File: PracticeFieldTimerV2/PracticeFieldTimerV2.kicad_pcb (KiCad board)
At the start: 2 copper layers, 99 x 96 mm, 37 parts, among them J1 External Controls, J2 Screw_Terminal_01x04, J3 Panel, J5 /CAN Enable, J6 RJ45-B, J7 RJ45-A, U1 ESP32-DevKitC, U4 DS3231MZ_TRL, U5 SN65HVD230DR

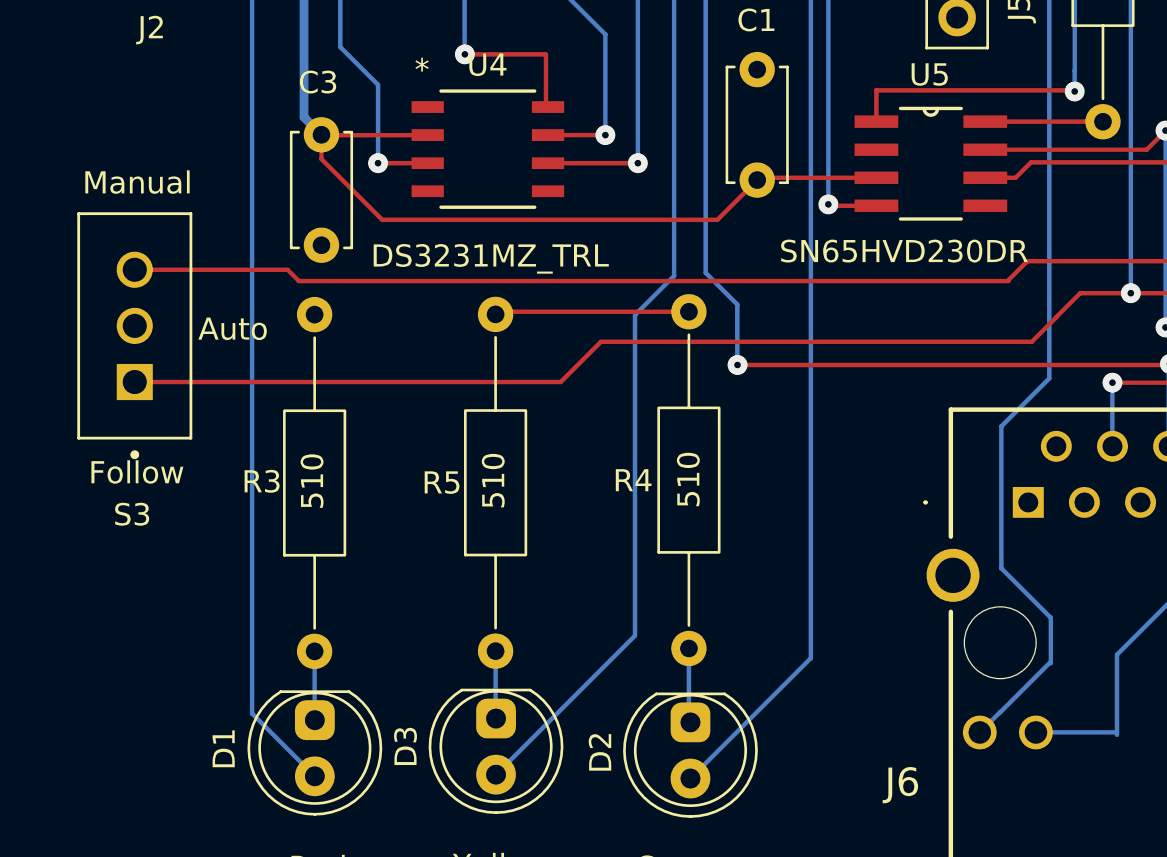
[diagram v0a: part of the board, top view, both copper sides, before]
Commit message: Add 10K pullup to SQW per DS3231 datasheet. Silly me!
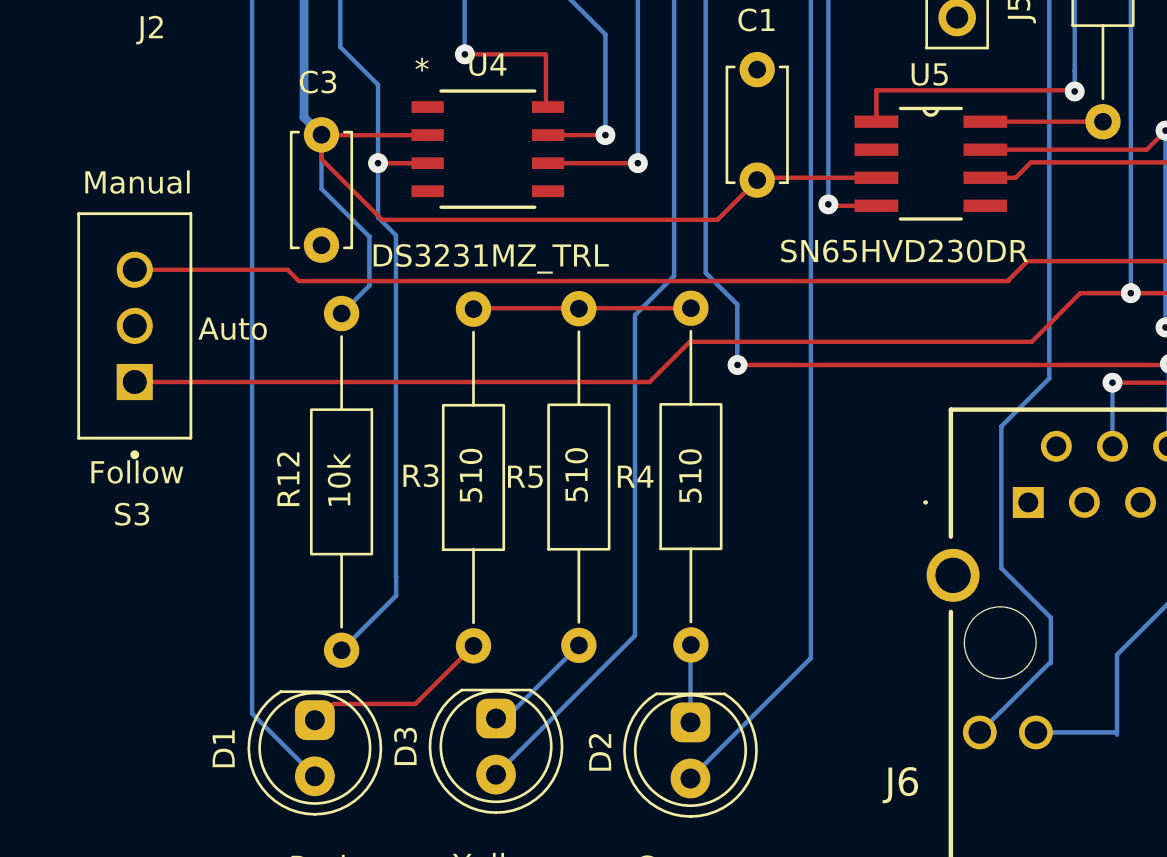
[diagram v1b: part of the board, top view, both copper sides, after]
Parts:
- added R12: 10k, Resistor_THT:R_Axial_DIN0207_L6.3mm_D2.5mm_P15.24mm_Horizontal, F.Cu at (63.5, 91.0)
- moved R3 7.19 mm to (69.5, 106.0)
- moved R5 3.78 mm to (74.2, 106.0)
- moved R4 0.18 mm to (79.3, 106.0)
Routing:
- net SQW: track 52.8 -> 76.2 mm
- net +3.3V: track 89.8 -> 99.3 mm
- net Net-(D1-K): track 3.10 -> 8.46 mm
- net Net-(D3-K): track 3.03 -> 4.68 mm
- net GND: track 8.62 -> 9.65 mm

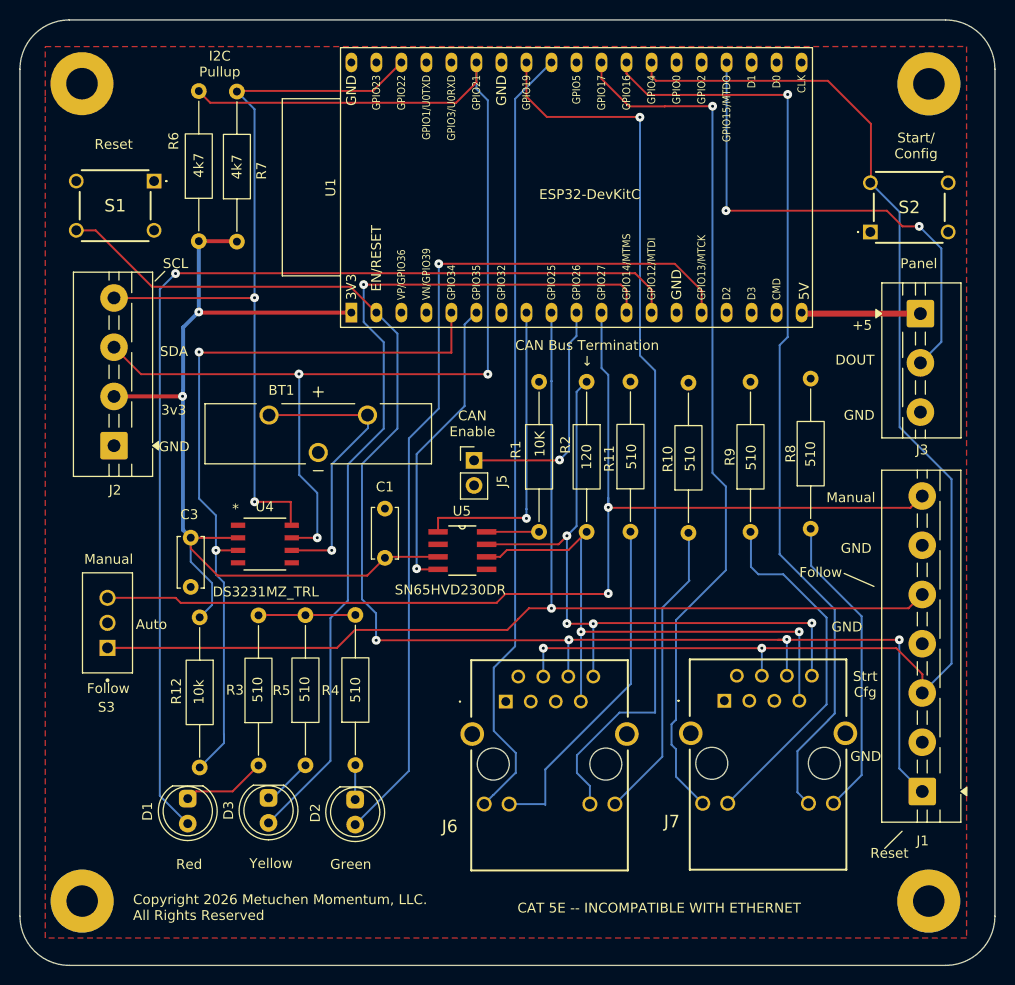
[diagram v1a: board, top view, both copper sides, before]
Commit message: Adjust traces to neaten layout a bit. Add bridge to unfilled area. Add meaningful reference codes to the mounting holes to eliminate duplicate footprint warnings.
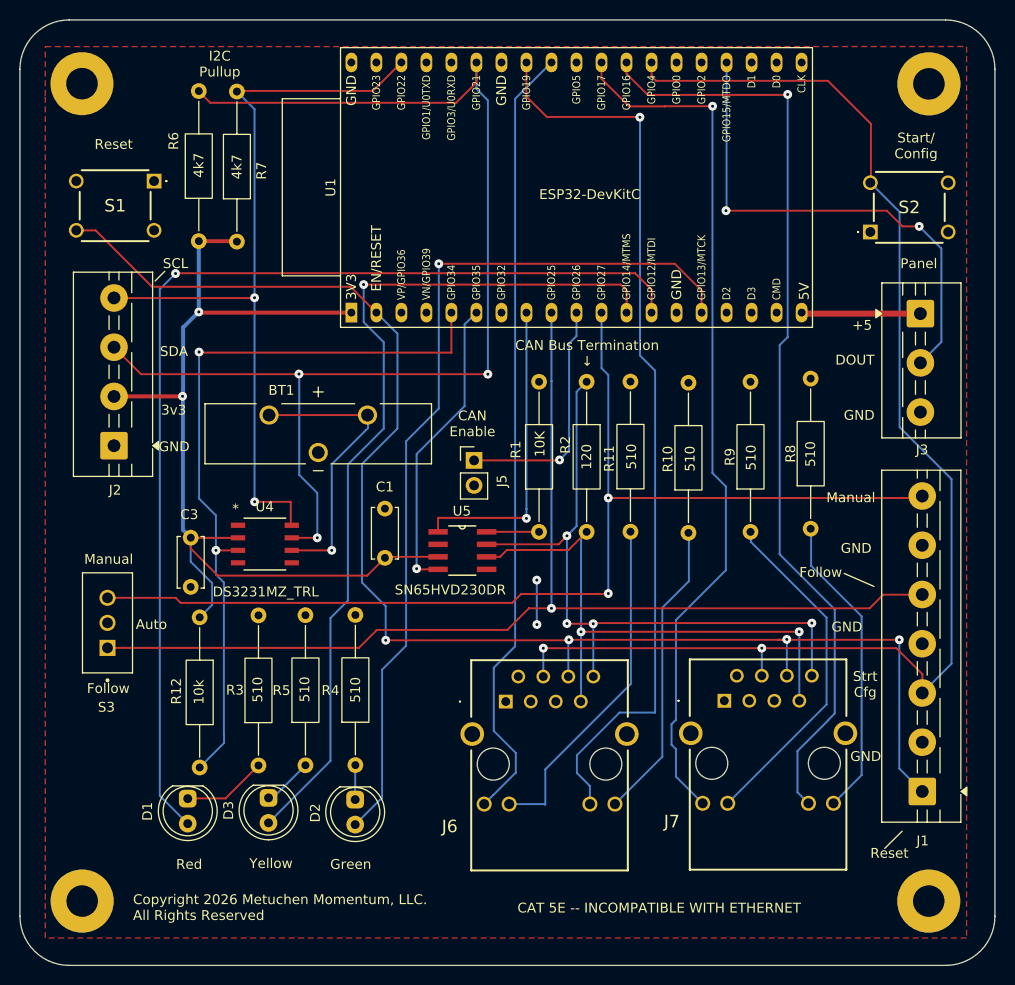
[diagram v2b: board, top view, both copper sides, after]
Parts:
- renumbered REF** to MH1, REF** to MH2, REF** to MH3, REF** to MH4
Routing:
- net GND: track 9.65 -> 4.54 mm, vias 0 -> 2
- net /Manual: track 113.1 -> 111.5 mm
- net Net-(J7-K_YELLOW): track 35.9 -> 34.4 mm
- net /RST: track 148.5 -> 148.0 mm
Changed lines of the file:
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@@
 		(descr "Mounting Hole 3.2mm, M3, generated by kicad-footprint-generator mountinghole.py")
 		(tags "mountinghole M3")
-		(property "Reference" "REF**"
+		(property "Reference" "MH2"
 			(at 0 -4.15 0)
 			(layer "F.SilkS")
@@
 		(descr "Mounting Hole 3.2mm, M3, generated by kicad-footprint-generator mountinghole.py")
 		(tags "mountinghole M3")
-		(property "Reference" "REF**"
+		(property "Reference" "MH3"
 			(at 0 -4.15 0)
 			(layer "F.SilkS")
@@
 		(descr "Mounting Hole 3.2mm, M3, generated by kicad-footprint-generator mountinghole.py")
 		(tags "mountinghole M3")
-		(property "Reference" "REF**"
+		(property "Reference" "MH1"
 			(at 0 -4.15 0)
 			(layer "F.SilkS")
@@
 		(descr "Mounting Hole 3.2mm, M3, generated by kicad-footprint-generator mountinghole.py")
 		(tags "mountinghole M3")
-		(property "Reference" "REF**"
+		(property "Reference" "MH4"
 			(at 0 -4.15 0)
 			(layer "F.SilkS")
@@
 		(net 1)
 	)
+	(via
+		(at 97.74 87.19)
+		(size 0.9)
+		(drill 0.3)
+		(layers "F.Cu" "B.Cu")
+		(free yes)
+		(net 2)
+	)
+	(via
+		(at 97.75 91.7)
+		(size 0.9)
+		(drill 0.3)
+		(layers "F.Cu" "B.Cu")
+		(free yes)
+		(net 2)
+	)
 	(segment
-		(start 79.54 90.73)
-		(end 69.89 90.73)
+		(start 97.74 91.63)
+		(end 97.81 91.7)
 		(width 0.2)
-		(layer "F.Cu")
+		(layer "B.Cu")
 		(net 2)
 	)
 	(segment
-		(start 66.85 108.64)
-		(end 63.15 108.64)
+		(start 97.74 87.19)
+		(end 97.74 91.63)
 		(width 0.2)
-		(layer "F.Cu")
-		(net 3)
+		(layer "B.Cu")
+		(net 2)
 	)
 	(segment
-		(start 63.15 108.64)
-		(end 62.415 109.375)
+		(start 69.48 106.01)
+		(end 66.14 109.35)
 		(width 0.2)
 		(layer "F.Cu")
@@
 	)
 	(segment
-		(start 69.48 106.01)
-		(end 66.85 108.64)
+		(start 66.14 109.35)
+		(end 62.44 109.35)
 		(width 0.2)
 		(layer "F.Cu")
@@
 	)
 	(segment
-		(start 84.75 72.81)
-		(end 84.75 106.565)
+		(start 82.03 109.285)
+		(end 79.3 112.015)
+		(width 0.2)
+		(layer "B.Cu")
+		(net 5)
+	)
+	(segment
+		(start 84.47 93.85)
+		(end 82.03 96.29)
+		(width 0.2)
+		(layer "B.Cu")
+		(net 5)
+	)
+	(segment
+		(start 87.79 69.77)
+		(end 84.47 73.09)
 		(width 0.2)
 		(layer "B.Cu")
@@
 	)
 	(segment
-		(start 84.75 106.565)
-		(end 79.3 112.015)
+		(start 84.47 73.09)
+		(end 84.47 93.85)
 		(width 0.2)
 		(layer "B.Cu")
@@
 	)
 	(segment
-		(start 87.79 69.77)
-		(end 84.75 72.81)
+		(start 82.03 96.29)
+		(end 82.03 109.285)
 		(width 0.2)
 		(layer "B.Cu")
@@
 	)
 	(segment
-		(start 54.15 94.07)
-		(end 77.45 94.07)
+		(start 132.91 88.67)
+		(end 136.86 88.67)
 		(width 0.2)
 		(layer "F.Cu")
@@
 	)
 	(segment
-		(start 77.45 94.07)
-		(end 79.27 92.25)
+		(start 95.85 91.14)
+		(end 96.94 90.05)
+		(width 0.2)
+		(layer "F.Cu")
+		(net 9)
+	)
+	(segment
+		(start 54.15 94.07)
+		(end 79.67 94.07)
 		(width 0.2)
 		(layer "F.Cu")
@@
 	)
 	(segment
-		(start 99.23 90.05)
-		(end 135.480001 90.049999)
+		(start 96.94 90.05)
+		(end 99.23 90.05)
 		(width 0.2)
 		(layer "F.Cu")
@@
 	)
 	(segment
-		(start 79.27 92.25)
-		(end 94.75 92.25)
+		(start 131.53 90.05)
+		(end 132.91 88.67)
 		(width 0.2)
 		(layer "F.Cu")
@@
 	)
 	(segment
-		(start 95.85 91.15)
-		(end 95.85 91.14)
+		(start 79.67 94.07)
+		(end 81.49 92.25)
 		(width 0.2)
 		(layer "F.Cu")
@@
 	)
 	(segment
-		(start 135.480001 90.049999)
-		(end 136.88 88.65)
+		(start 99.23 90.05)
+		(end 131.53 90.05)
 		(width 0.2)
 		(layer "F.Cu")
@@
 	)
 	(segment
-		(start 96.94 90.05)
-		(end 99.23 90.05)
+		(start 95.85 91.15)
+		(end 95.85 91.14)
 		(width 0.2)
 		(layer "F.Cu")
@@
 	)
 	(segment
-		(start 95.85 91.14)
-		(end 96.94 90.05)
+		(start 81.49 92.25)
+		(end 94.75 92.25)
 		(width 0.2)
 		(layer "F.Cu")
@@
 	)
 	(segment
-		(start 61.07 88.99)
-		(end 61.58 89.5)
-		(width 0.2)
-		(layer "F.Cu")
-		(net 10)
-	)
-	(segment
 		(start 54.15 88.99)
 		(end 61.07 88.99)
@@
 	)
 	(segment
-		(start 94.55 88.6)
-		(end 93.7 89.45)
-		(width 0.2)
-		(layer "F.Cu")
-		(net 10)
-	)
-	(segment
-		(start 104.55 88.6)
-		(end 94.55 88.6)
+		(start 61.07 88.99)
+		(end 61.58 89.5)
 		(width 0.2)
 		(layer "F.Cu")
@@
 	)
 	(segment
-		(start 105.05 79.85)
-		(end 135.68 79.85)
+		(start 61.58 89.5)
+		(end 95.25 89.5)
 		(width 0.2)
 		(layer "F.Cu")
@@
 	)
 	(segment
-		(start 105 79.8)
-		(end 105.05 79.85)
+		(start 96.15 88.6)
+		(end 95.25 89.5)
 		(width 0.2)
 		(layer "F.Cu")
@@
 	)
 	(segment
-		(start 61.58 89.5)
-		(end 93.7 89.5)
+		(start 104.55 88.6)
+		(end 96.15 88.6)
 		(width 0.2)
 		(layer "F.Cu")
@@
 	)
 	(segment
-		(start 135.68 79.85)
-		(end 136.88 78.65)
+		(start 105 78.85)
+		(end 136.68 78.85)
 		(width 0.2)
 		(layer "F.Cu")
@@
 	)
 	(via
-		(at 105 79.8)
+		(at 105 78.85)
 		(size 0.9)
 		(drill 0.3)
@@
 	)
 	(segment
-		(start 105 79.8)
-		(end 105 78.85)
-		(width 0.2)
-		(layer "B.Cu")
-		(net 10)
-	)
-	(segment
 		(start 104.31272 65.66272)
 		(end 104.31272 60.02632)
@@
 	)
 	(segment
-		(start 81.43 93.3)
-		(end 100.95 93.3)
-		(width 0.2)
-		(layer "F.Cu")
-		(net 12)
-	)
-	(segment
 		(start 52.96 51.68)
 		(end 58.68 57.4)
@@
 	)
 	(segment
-		(start 100.95 93.3)
-		(end 101 93.25)
+		(start 122.25 93.25)
+		(end 123.09 93.25)
 		(width 0.2)
 		(layer "F.Cu")
@@
 	(segment
 		(start 122.25 93.25)
-		(end 123.09 93.25)
+		(end 134.55 93.25)
 		(width 0.2)
 		(layer "F.Cu")
@@
 	)
 	(segment
-		(start 122.25 93.25)
-		(end 134.55 93.25)
+		(start 100.95 93.3)
+		(end 101 93.25)
 		(width 0.2)
 		(layer "F.Cu")
@@
 	)
 	(segment
+		(start 82.4 93.3)
+		(end 100.95 93.3)
+		(width 0.2)
+		(layer "F.Cu")
+		(net 12)
+	)
+	(segment
 		(start 78.8264 57.4)
 		(end 81.45272 60.02632)
@@
 	)
 	(via
-		(at 81.43 93.3)
+		(at 82.4 93.3)
 		(size 0.9)
 		(drill 0.3)
@@
 	)
 	(segment
-		(start 81.42 93.29)
-		(end 81.42 90.56)
-		(width 0.2)
-		(layer "B.Cu")
-		(net 12)
-	)
-	(segment
-		(start 79.99 89.13)
-		(end 79.99 75.4)
+		(start 83.59 71.8)
+		(end 83.59 62.1636)
 		(width 0.2)
 		(layer "B.Cu")
@@
 	)
 	(segment
-		(start 81.43 93.3)
-		(end 81.42 93.29)
+		(start 79.99 75.4)
+		(end 83.59 71.8)
 		(width 0.2)
 		(layer "B.Cu")
@@
 	)
 	(segment
-		(start 81.42 90.56)
-		(end 79.99 89.13)
+		(start 83.59 62.1636)
+		(end 81.45272 60.02632)
 		(width 0.2)
 		(layer "B.Cu")
@@
 	)
 	(segment
-		(start 79.99 75.4)
-		(end 83.59 71.8)
+		(start 79.99 87.43)
+		(end 79.99 75.4)
 		(width 0.2)
 		(layer "B.Cu")
@@
 	)
 	(segment
-		(start 83.59 62.1636)
-		(end 81.45272 60.02632)
+		(start 82.4 89.84)
+		(end 79.99 87.43)
 		(width 0.2)
 		(layer "B.Cu")
@@
 	)
 	(segment
-		(start 123.13 96.9)
-		(end 123.13 93.21)
+		(start 82.4 93.3)
+		(end 82.4 89.84)
 		(width 0.2)
 		(layer "B.Cu")
@@
 	)
 	(segment
-		(start 83.59 71.8)
-		(end 83.59 62.1636)
+		(start 123.13 96.9)
+		(end 123.13 93.21)
 		(width 0.2)
 		(layer "B.Cu")
@@
 	(segment
 		(start 113.185 82.87)
-		(end 113.185 87.17)
+		(end 113.185 87.295)
+		(width 0.2)
+		(layer "B.Cu")
+		(net 27)
+	)
+	(segment
+		(start 113.185 87.295)
+		(end 113.1875 87.2975)
 		(width 0.2)
 		(layer "B.Cu")
@@
 	)
 	(segment
-		(start 113.25 87.235)
+		(start 113.185 87.3)
 		(end 110.485 90)
 		(width 0.2)
@@
 	)
 	(segment
-		(start 127.165 99.81)
-		(end 127.165 91)
-		(width 0.2)
-		(layer "B.Cu")
-		(net 49)
-	)
-	(segment
 		(start 119.485 82.77)
-		(end 119.485 85.84)
+		(end 119.485 83.32)
 		(width 0.2)
 		(layer "B.Cu")
@@
 	)
 	(segment
-		(start 119.485 85.84)
-		(end 120.245 86.6)
+		(start 119.485 83.32)
+		(end 127.165 91)
 		(width 0.2)
 		(layer "B.Cu")
@@
 	)
 	(segment
-		(start 122.765 86.6)
-		(end 120.245 86.6)
+		(start 127.165 99.81)
+		(end 117.125 109.85)
 		(width 0.2)
 		(layer "B.Cu")
@@
 	(segment
 		(start 127.165 91)
-		(end 122.765 86.6)
-		(width 0.2)
-		(layer "B.Cu")
-		(net 49)
-	)
-	(segment
-		(start 117.125 109.85)
 		(end 127.165 99.81)
 		(width 0.2)

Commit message: Tidy the schematic. Ground both common pins on push buttons.
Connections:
- S1 pad 2: unconnected-(S1-COM_2-Pad2) -> GND
- S2 pad 1: unconnected-(S2-COM_1-Pad1) -> GND

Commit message: Minor faffing about with reference numbers.
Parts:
- gave numbers to parts that had none: 1
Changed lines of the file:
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@@
 		(layer "F.Cu")
 		(at 137.54 119.79)
-		(property "Reference" ""
+		(property "Reference" "MH3"
 			(at 0 0 0)
 			(layer "F.SilkS")

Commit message: Add version number and perform final cleanup prior to requesting fab quotes.
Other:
- board text added: "Version 1.0.0 14-Jun-2026"
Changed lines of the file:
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@@
 	)
 	(gr_text "Manual"
-		(at 129.63 78.81 0)
+		(at 129.62 80.19 0)
 		(layer "F.SilkS")
 		(effects
@@
 		)
 	)
+	(gr_text "Version 1.0.0\n14-Jun-2026"
+		(at 51.07 105.4 0)
+		(layer "F.SilkS")
+		(effects
+			(font
+				(size 1 1)
+				(thickness 0.15)
+			)
+			(justify left bottom)
+		)
+	)
